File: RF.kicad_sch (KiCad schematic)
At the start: 41 parts, among them J10 Conn_01x01_Pin, J11 Conn_01x01_Pin, J12 Conn_01x01_Pin, Q19 NMOS, Q20 NMOS, Q21 NMOS, Q22 NMOS, Q23 NMOS, Q24 NMOS, U7 OPA2196xDGK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

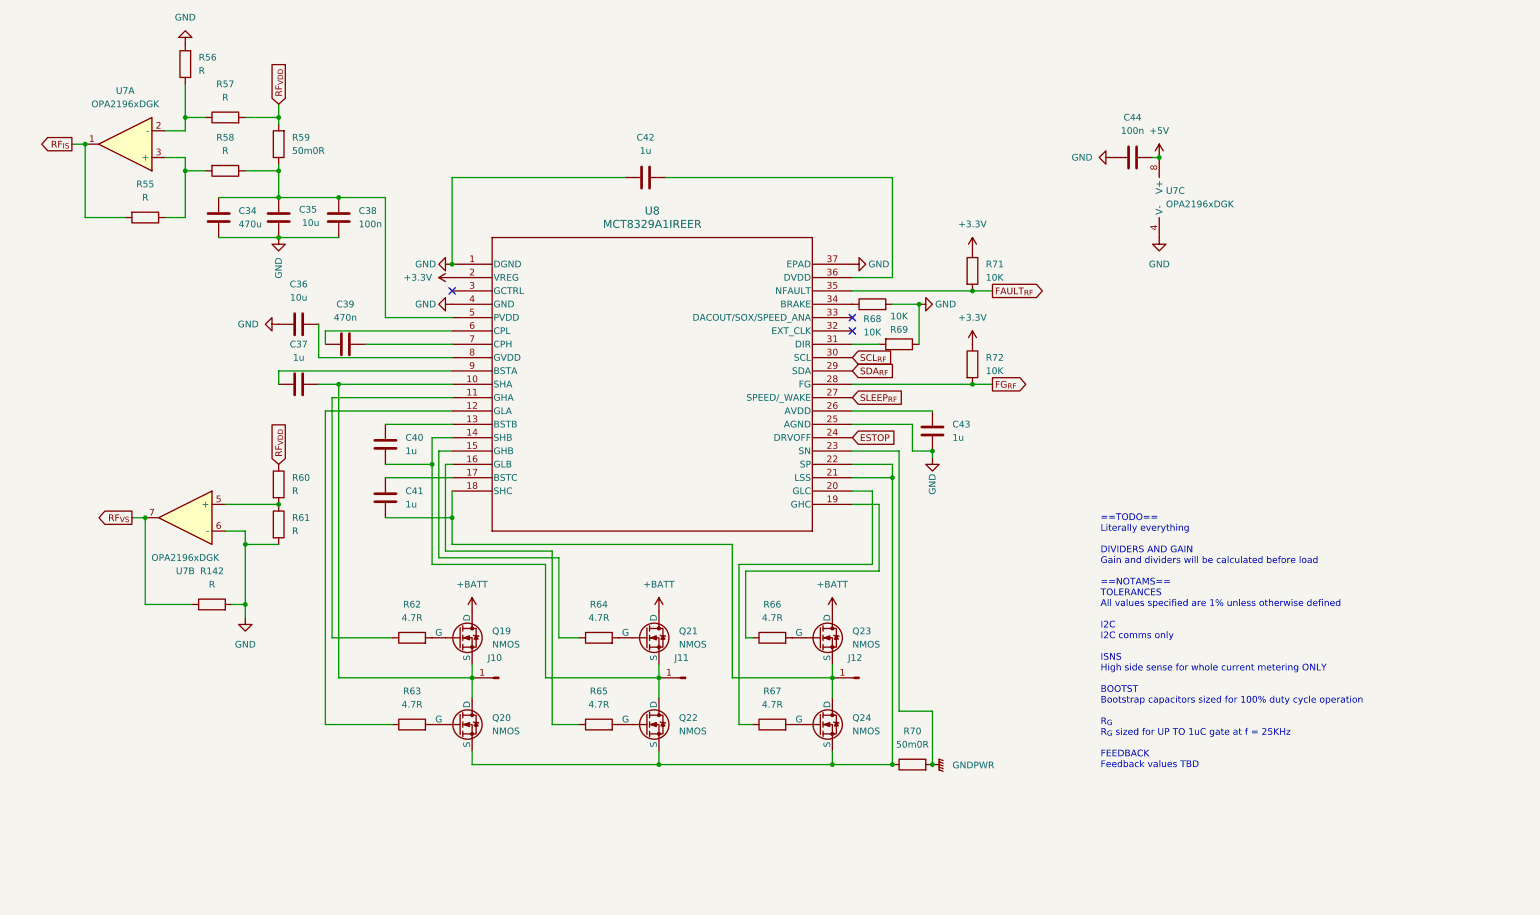
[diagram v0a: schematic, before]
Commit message: The great decluttering
Moved all possible controls to I2C, part selection commenced, IOs assigned pending comms schema
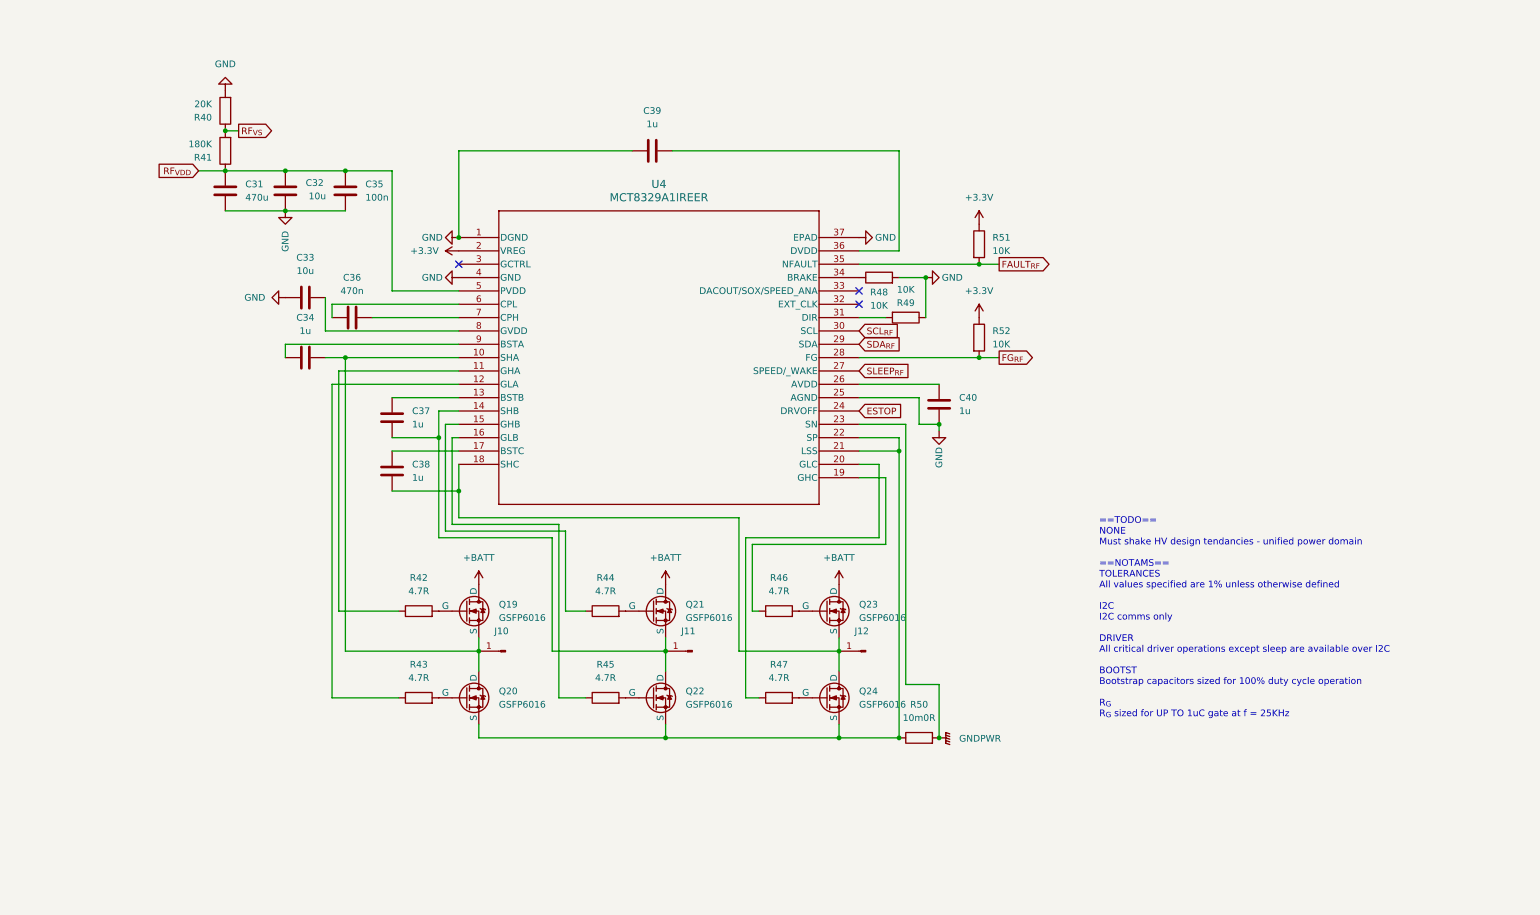
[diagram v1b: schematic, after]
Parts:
- removed C41, C42, C43: 1u, Capacitor_SMD:C_0603_1608Metric, symbol Device:C
- removed C44: 100n, Capacitor_SMD:C_0603_1608Metric, symbol Device:C
- removed R142, R55, R56, R57, R58, R60, R61: R, Resistor_SMD:R_0603_1608Metric_Pad0.98x0.95mm_HandSolder, symbol Device:R
- removed R59, R70: 50m0R, Resistor_SMD:R_1206_3216Metric, symbol Device:R
- removed R62, R63, R64, R65, R66, R67: 4.7R, Resistor_SMD:R_1206_3216Metric, symbol Device:R
- removed R68, R69, R71, R72: 10K, Resistor_SMD:R_0603_1608Metric_Pad0.98x0.95mm_HandSolder, symbol Device:R
- removed U7: OPA2196xDGK, Package_SO:VSSOP-8_3x3mm_P0.65mm, symbol Amplifier_Operational:OPA2196xDGK
- removed U8: MCT8329A1IREER, footprints:WQFN36_REE_TEX, symbol MCT8329:MCT8329A1IREER
- added C31: 470u, Capacitor_SMD:C_0603_1608Metric, symbol Device:C
- added C32, C33: 10u, Capacitor_SMD:C_0603_1608Metric, symbol Device:C
- added R40: 20K, Resistor_SMD:R_0603_1608Metric_Pad0.98x0.95mm_HandSolder, symbol Device:R
- added R41: 180K, Resistor_SMD:R_0603_1608Metric_Pad0.98x0.95mm_HandSolder, symbol Device:R
- added R42, R43, R44, R45, R46, R47: 4.7R, Resistor_SMD:R_1206_3216Metric, symbol Device:R
- added R48, R49, R51, R52: 10K, Resistor_SMD:R_0603_1608Metric_Pad0.98x0.95mm_HandSolder, symbol Device:R
- added R50: 10m0R, Resistor_SMD:R_1206_3216Metric, symbol Device:R
- added U4: MCT8329A1IREER, footprints:WQFN36_REE_TEX, symbol MCT8329:MCT8329A1IREER
- C34: value 470u -> 1u
- C35: value 10u -> 100n
- C36: value 10u -> 470n
- C38: value 100n -> 1u
- C39: value 470n -> 1u
- Q19, Q20, Q21, Q22, Q23, Q24: value NMOS -> GSFP6016; footprint (none) -> Package_DFN_QFN:PQFN-8-EP_6x5mm_P1.27mm_Generic
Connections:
- net +3.3V: now also R51.1, R52.1, U4.2 (VREG)
- net ESTOP: now also U4.24 (DRVOFF)
- net FAULT_{RF}: now also R51.2, U4.35 (NFAULT)
- net FG_{RF}: now also R52.2, U4.28 (FG)
- net GND: now also C39.1, C40.1, C31.2, C32.2, C33.1, R40.2, R48.2, R49.1, U4.1 (DGND), U4.25 (AGND), U4.37 (EPAD), U4.4 (GND); no longer C34.2, C36.1, C38.2
- net GNDPWR: now also R50.2, U4.23 (SN)
- net RF_{VDD}: now also C35.1, C31.1, C32.1, R41.1, U4.5 (PVDD)
- net RF_{VS}: now also R40.1, R41.2
- net SCL_{RF}: now also U4.30 (SCL)
- net SDA_{RF}: now also U4.29 (SDA)
- net SLEEP_{RF}: now also U4.27 (SPEED/_WAKE)
- net at J10.1 (Pin_1), Q19.3 (S), Q20.1 (D): now also C34.1, U4.10 (SHA); no longer C37.1
- net at J11.1 (Pin_1), Q21.3 (S), Q22.1 (D): now also C37.2, U4.14 (SHB); no longer C40.2
- net at J12.1 (Pin_1), Q23.3 (S), Q24.1 (D): now also C38.2, U4.18 (SHC)
- net at Q20.3 (S), Q22.3 (S), Q24.3 (S): now also R50.1, U4.21 (LSS), U4.22 (SP)
- net at C39.2: now also U4.36 (DVDD)
- net at C36.2: now also U4.7 (CPH)
- net at Q20.2 (G): now also R43.2
- net at Q23.2 (G): now also R46.2
- net at Q19.2 (G): now also R42.2
- net at Q22.2 (G): now also R45.2
- net at Q24.2 (G): now also R47.2
- net at Q21.2 (G): now also R44.2
- new net: R44.1, U4.15 (GHB)
- new net: R46.1, U4.19 (GHC)
- new net: C38.1, U4.17 (BSTC)
- new net: C33.2, U4.8 (GVDD)
- new net: R49.2, U4.31 (DIR)
- new net: R45.1, U4.16 (GLB)
- new net: R42.1, U4.11 (GHA)
- new net: C36.1, U4.6 (CPL)
- new net: C37.1, U4.13 (BSTB)
- new net: R43.1, U4.12 (GLA)
- new net: R47.1, U4.20 (GLC)
- new net: C40.2, U4.26 (AVDD)
- new net: R48.1, U4.34 (BRAKE)
- new net: C34.2, U4.9 (BSTA)
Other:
- note added: "==TODO== NONE Must shake HV design tendancies - unified power domain ==NOTAMS== TOLERANCES All values specified are 1% unless otherwise defined I2C I2C comms only DRIVER All critical driver operations except sleep are available over I2C BOOTST Bootstrap capacitors sized for 100% duty cycle operation R_{G} R_{G} sized for UP TO 1uC gate at f = 25KHz"
- note removed: "==TODO== Literally everything DIVIDERS AND GAIN Gain and dividers will be calculated before load ==NOTAMS== TOLERANCES All values specified are 1% unless otherwise defined I2C I2C comms only ISNS High side sense for whole current metering ONLY BOOTST Bootstrap capacitors sized for 100% duty cycle operation R_{G} R_{G} sized for UP TO 1uC gate at f = 25KHz FEEDBACK Feedback values TBD"

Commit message: Powerstage
Powerstage layout, non critical changes to schematic
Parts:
- removed C35: 100n, Capacitor_SMD:C_0603_1608Metric, symbol Device:C
- removed J10, J11, J12: Conn_01x01_Pin, symbol Connector:Conn_01x01_Pin
- removed Q19, Q20, Q21, Q22, Q23, Q24: GSFP6016, Package_DFN_QFN:PQFN-8-EP_6x5mm_P1.27mm_Generic, symbol Simulation_SPICE:NMOS
- removed R50: 10m0R, Resistor_SMD:R_1206_3216Metric, symbol Device:R
- added J4: 1724470408, footprints:CONN08_1724470408_MOL, symbol 1724470408:1724470408
- added Q19, Q20, Q21, Q22, Q23, Q24: GSFP6016, Package_SO:PowerPAK_SO-8_Single, symbol Transistor_FET:SiR696DP
- added R50: WSL3637R0100FEA, WSL3637_VIS, symbol WSL3637R0100FEA:WSL3637R0100FEA
- C31: footprint Capacitor_SMD:C_0603_1608Metric -> Capacitor_THT:CP_Radial_D10.0mm_P5.00mm
- C32: footprint Capacitor_SMD:C_0603_1608Metric -> Capacitor_SMD:C_1210_3225Metric
- C33: footprint Capacitor_SMD:C_0603_1608Metric -> Capacitor_SMD:C_0402_1005Metric
- C34, C36, C37, C38, C39, C40: footprint Capacitor_SMD:C_0603_1608Metric -> Capacitor_SMD:C_0201_0603Metric
- R40, R41, R48, R49, R51, R52: footprint Resistor_SMD:R_0603_1608Metric_Pad0.98x0.95mm_HandSolder -> Resistor_SMD:R_0201_0603Metric
- R42, R43, R44, R45, R46, R47: value 4.7R -> 4R7; footprint Resistor_SMD:R_1206_3216Metric -> Resistor_SMD:R_0603_1608Metric
- U4: footprint footprints:WQFN36_REE_TEX -> WQFN36_REE_TEX
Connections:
- net GNDPWR: now also J4.4, J4.8, R50.4; no longer U4.23 (SN)
- net RF_{VDD}: now also Q19.5 (D), Q21.5 (D), Q23.5 (D)
- net at R44.2: now also Q21.4 (G)
- net at C37.2, U4.14 (SHB): now also J4.2, J4.6, Q21.1 (S), Q21.2 (S), Q21.3 (S), Q22.5 (D)
- net at R46.2: now also Q23.4 (G)
- net at R42.2: now also Q19.4 (G)
- net at C34.1, U4.10 (SHA): now also J4.1, J4.5, Q19.1 (S), Q19.2 (S), Q19.3 (S), Q20.5 (D)
- net at C38.2, U4.18 (SHC): now also J4.3, J4.7, Q23.1 (S), Q23.2 (S), Q23.3 (S), Q24.5 (D)
- net at R45.2: now also Q22.4 (G)
- net at U4.6 (CPL): now also C36.2; no longer C36.1
- net at U4.7 (CPH): now also C36.1; no longer C36.2
- net at U4.21 (LSS), U4.22 (SP): now also R50.2
- net at R43.2: now also Q20.4 (G)
- net at R47.2: now also Q24.4 (G)
- new net: Q20.1 (S), Q20.2 (S), Q20.3 (S), Q22.1 (S), Q22.2 (S), Q22.3 (S), Q24.1 (S), Q24.2 (S), Q24.3 (S), R50.1
- new net: R50.3, U4.23 (SN)
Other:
- note added: "==TODO== NONE Must shake HV design tendancies - unified power domain ==NOTAMS== TOLERANCES All values specified are 1% unless otherwise defined I2C I2C comms only DRIVER All critical driver operations except sleep are available over I2C BOOTST Bootstrap capacitors sized for 100% duty cycle operation R_{G} R_{G} sized for UP TO 1uC gate at f = 25KHz SUBSTRATE TEMP PCB will not comply with IEC boar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"
- note removed: "==TODO== NONE Must shake HV design tendancies - unified power domain ==NOTAMS== TOLERANCES All values specified are 1% unless otherwise defined I2C I2C comms only DRIVER All critical driver operations except sleep are available over I2C BOOTST Bootstrap capacitors sized for 100% duty cycle operation R_{G} R_{G} sized for UP TO 1uC gate at f = 25KHz"
